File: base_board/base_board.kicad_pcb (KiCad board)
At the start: 6 copper layers, 52 parts, among them J1 Conn_ARM_JTAG_SWD_20, SW1 SW_Push, U1 STM32F446ZEJx, U2 IS42S16400J-xT, U3 BMI270, U4 USB_C_Receptacle_USB2.0, U5 10p, U6 10p, U7 LD3985M33R_SOT23, Y1 Crystal_GND24

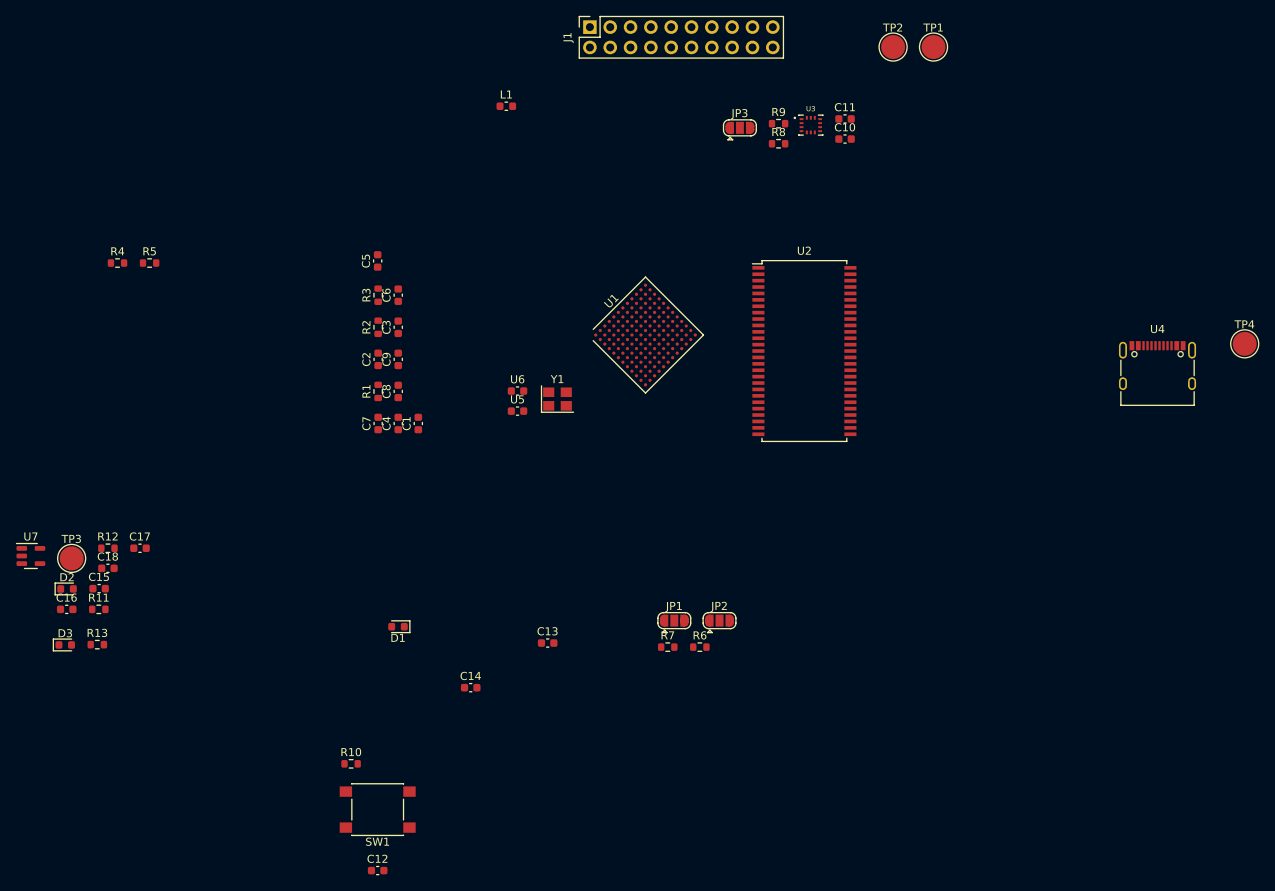
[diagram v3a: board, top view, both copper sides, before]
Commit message: [pcb] draft of components layout
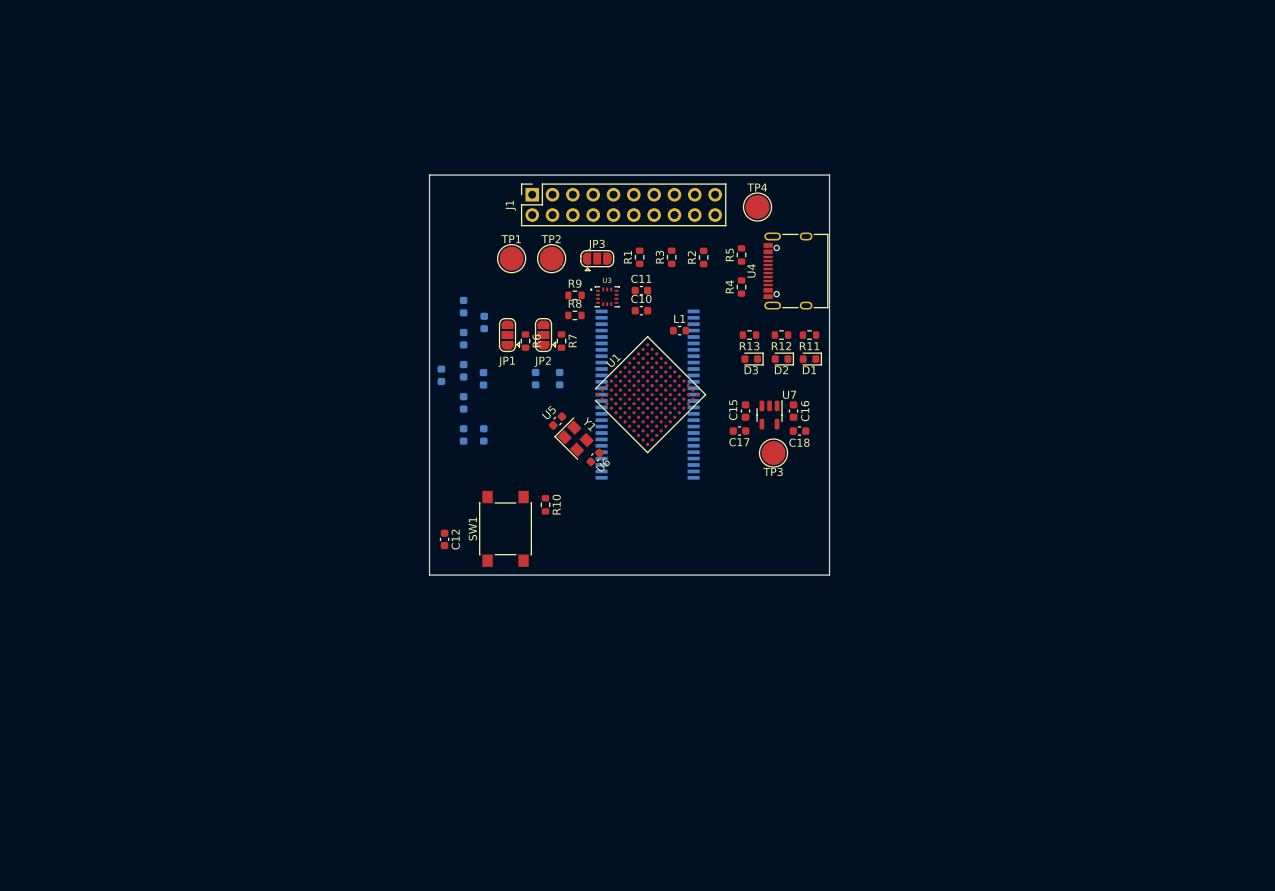
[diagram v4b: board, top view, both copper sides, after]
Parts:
- C1, C13, C14, C2, C3, C4, C5, C6, C7, C8, C9, U2: moved to B.Cu
- moved R11 95.2 mm to (150.5, 88.0), turned to 180 degrees
- moved C16 94.2 mm to (148.5, 97.5), turned to 90 degrees
- moved U7 94.0 mm to (145.5, 98.0), turned to -90 degrees
- moved D2 93.8 mm to (147.0, 91.0), turned to 180 degrees
- moved D3 92.9 mm to (143.2, 91.0), turned to 180 degrees
- moved R13 90.2 mm to (143.0, 88.0), turned to 180 degrees
- moved TP3 88.7 mm to (146.0, 102.8), turned to 180 degrees
- moved R12 88.3 mm to (147.0, 88.0), turned to 180 degrees
- moved C18 88.1 mm to (149.2, 100.0)
- moved C15 83.8 mm to (142.5, 97.5), turned to -90 degrees
- moved R4 78.1 mm to (142.0, 82.0), turned to 90 degrees
- moved C17 76.4 mm to (141.8, 100.0), turned to 180 degrees
- moved R5 74.0 mm to (142.0, 78.0), turned to 90 degrees
- moved TP4 63.3 mm to (144.0, 72.0)
- moved D1 61.4 mm to (150.5, 91.0)
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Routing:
- net /HSE_OUT: track 0.00 -> 0.67 mm
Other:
- board outline added: 50 x 50 mm

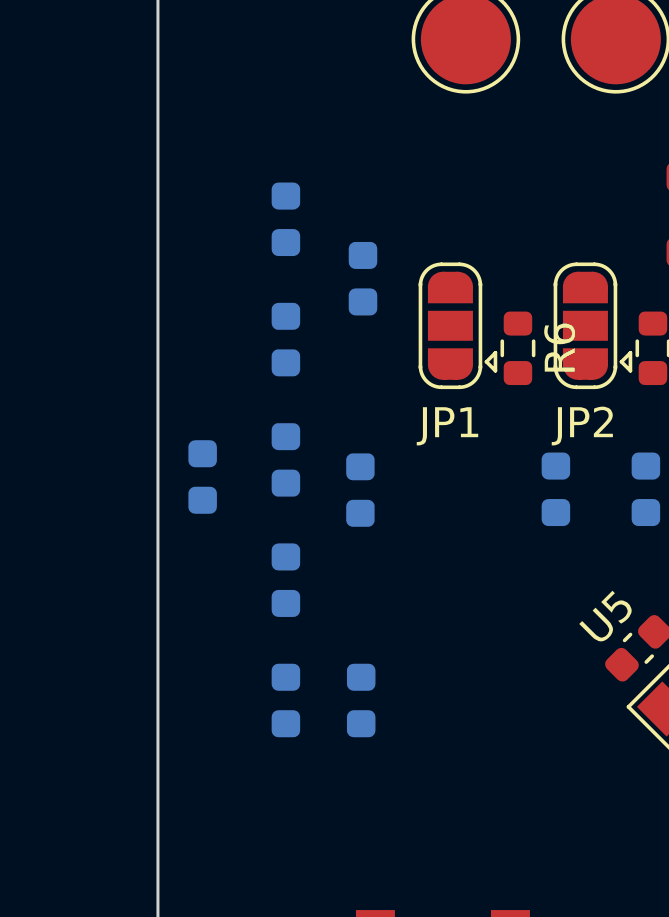
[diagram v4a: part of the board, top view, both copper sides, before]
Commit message: [pcb] changed capacitors layer
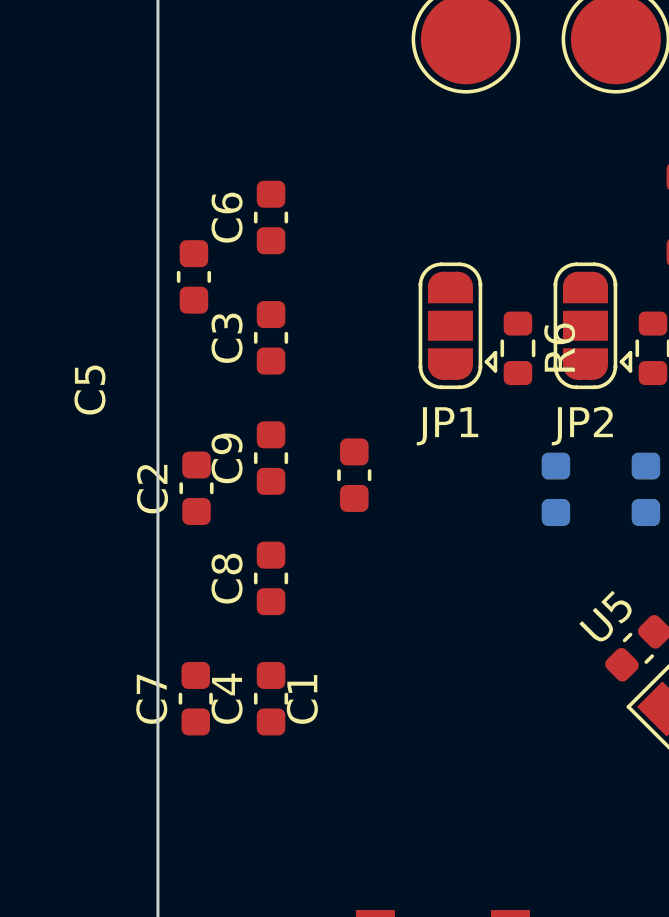
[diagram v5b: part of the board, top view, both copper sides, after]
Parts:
- C1, C2, C3, C4, C5, C6, C7, C8, C9: moved to F.Cu
- moved C5 5.64 mm to (104.2, 86.4)
- moved C7 5.52 mm to (104.3, 100.4)
- moved C2 5.47 mm to (104.3, 93.4)
- moved C1 5.06 mm to (109.5, 93.0)
- moved C6 0.50 mm to (106.8, 84.4)
- moved C8 0.50 mm to (106.8, 96.4)
- moved C9 0.50 mm to (106.8, 92.4)
- moved C3 0.50 mm to (106.8, 88.4)
- moved C4 0.50 mm to (106.8, 100.4)

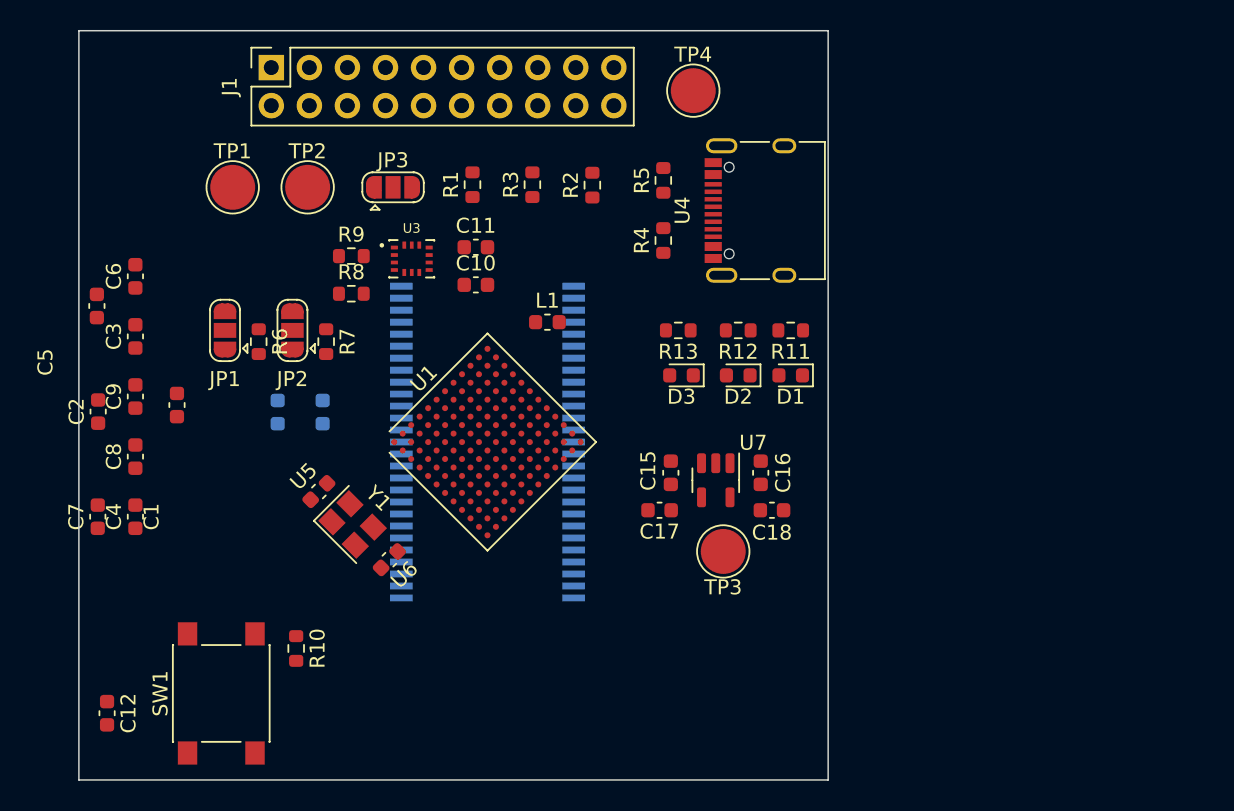
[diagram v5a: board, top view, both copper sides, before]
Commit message: [pcb][schematic] added gpio headers&sockets
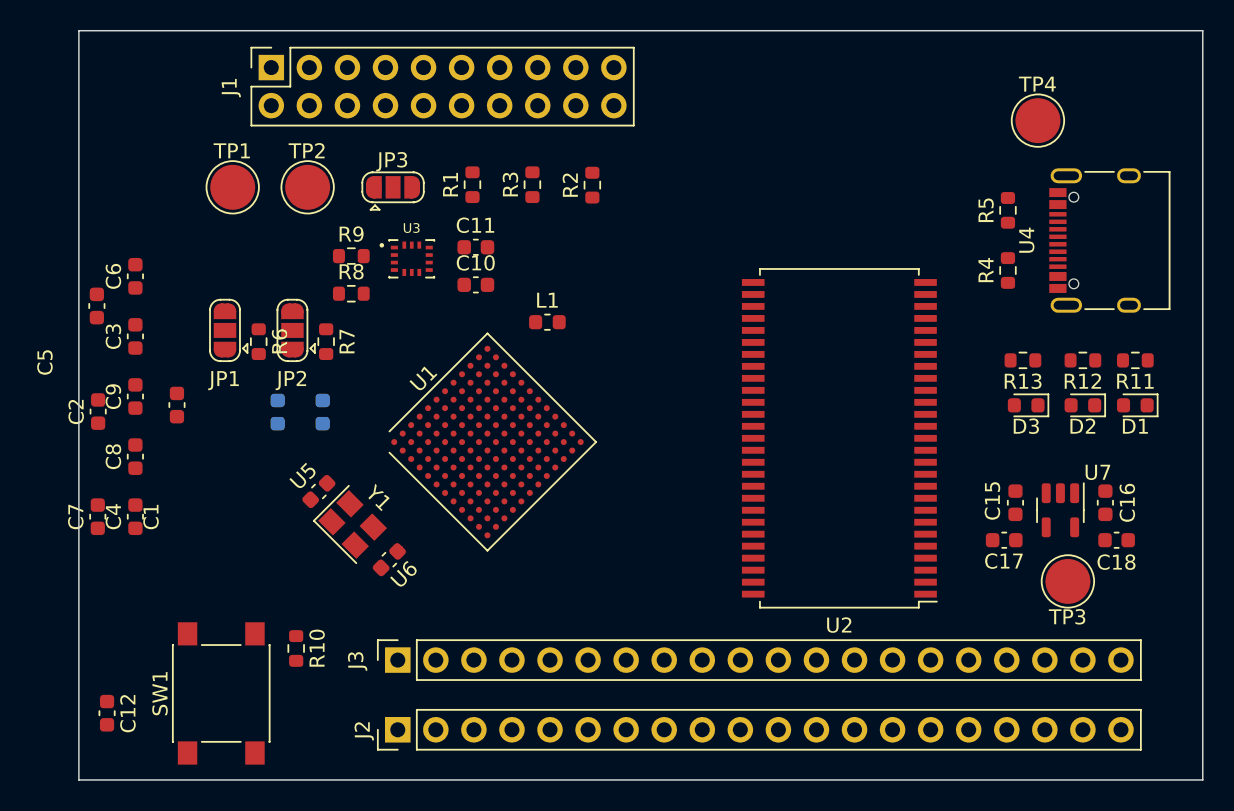
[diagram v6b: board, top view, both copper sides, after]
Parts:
- added J2: Conn_01x20_Pin, Connector_PinHeader_2.54mm:PinHeader_1x20_P2.54mm_Vertical, F.Cu at (124.3, 114.7)
- added J3: Conn_01x20_Socket, Connector_PinSocket_2.54mm:PinSocket_1x20_P2.54mm_Vertical, F.Cu at (124.3, 110.0)
- U2: moved to F.Cu
- moved U2 23.5 mm to (153.8, 95.2), turned to 180 degrees
- moved C15 23.1 mm to (165.5, 99.5)
- moved C16 23.1 mm to (171.5, 99.5)
- moved C17 23.1 mm to (164.8, 102.0)
- moved C18 23.1 mm to (172.2, 102.0)
- moved D1 23.1 mm to (173.5, 93.0)
- moved D2 23.1 mm to (170.0, 93.0)
- moved D3 23.1 mm to (166.2, 93.0)
- moved R11 23.1 mm to (173.5, 90.0)
- moved R12 23.1 mm to (170.0, 90.0)
- moved R13 23.1 mm to (166.0, 90.0)
- moved R4 23.1 mm to (165.0, 84.0)
- moved R5 23.1 mm to (165.0, 80.0)
- moved TP3 23.1 mm to (169.0, 104.8)
- moved TP4 23.1 mm to (167.0, 74.0)
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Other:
- board size 50 x 50 mm -> 75 x 50 mm

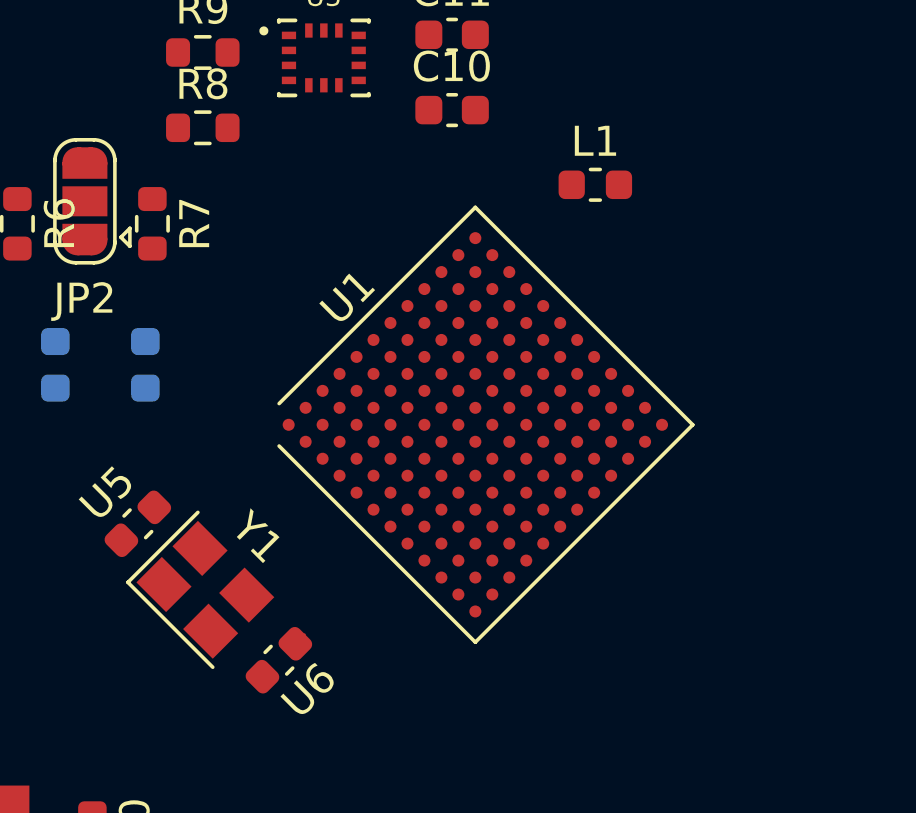
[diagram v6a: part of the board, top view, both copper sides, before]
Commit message: [pcb] added part of bga route
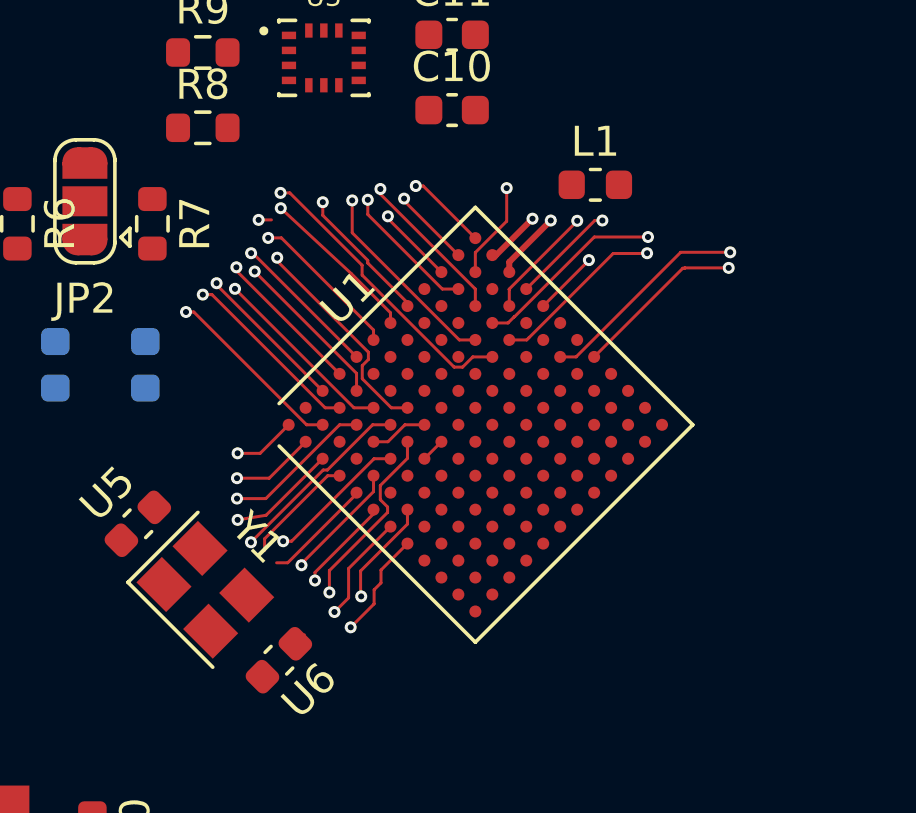
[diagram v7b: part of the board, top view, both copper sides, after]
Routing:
- net /PD2: track 0.00 -> 9.80 mm, vias 0 -> 1
- net /BOOT0: track 0.00 -> 7.29 mm, vias 0 -> 1
- net /FMC_SDCLK: track 0.00 -> 7.11 mm, vias 0 -> 1
- net /PD3: track 0.00 -> 6.66 mm, vias 0 -> 1
- net /FMC_D3: track 0.00 -> 6.40 mm, vias 0 -> 1
- net /FMC_A5: track 0.00 -> 6.30 mm, vias 0 -> 1
- net /FMC_A2: track 0.00 -> 6.27 mm, vias 0 -> 1
- net /FMC_A1: track 0.00 -> 6.26 mm, vias 0 -> 1
- net /PE5: track 0.00 -> 6.12 mm, vias 0 -> 1
- net /PE4: track 0.00 -> 6.11 mm, vias 0 -> 1
- net /FMC_D2: track 0.00 -> 5.79 mm, vias 0 -> 1
- net /FMC_BA1: track 0.00 -> 5.71 mm, vias 0 -> 1
- net /SWO: track 0.00 -> 5.39 mm, vias 0 -> 1
- net /PE6: track 0.00 -> 5.38 mm, vias 0 -> 1
- net /PC12: track 0.00 -> 5.21 mm, vias 0 -> 1
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
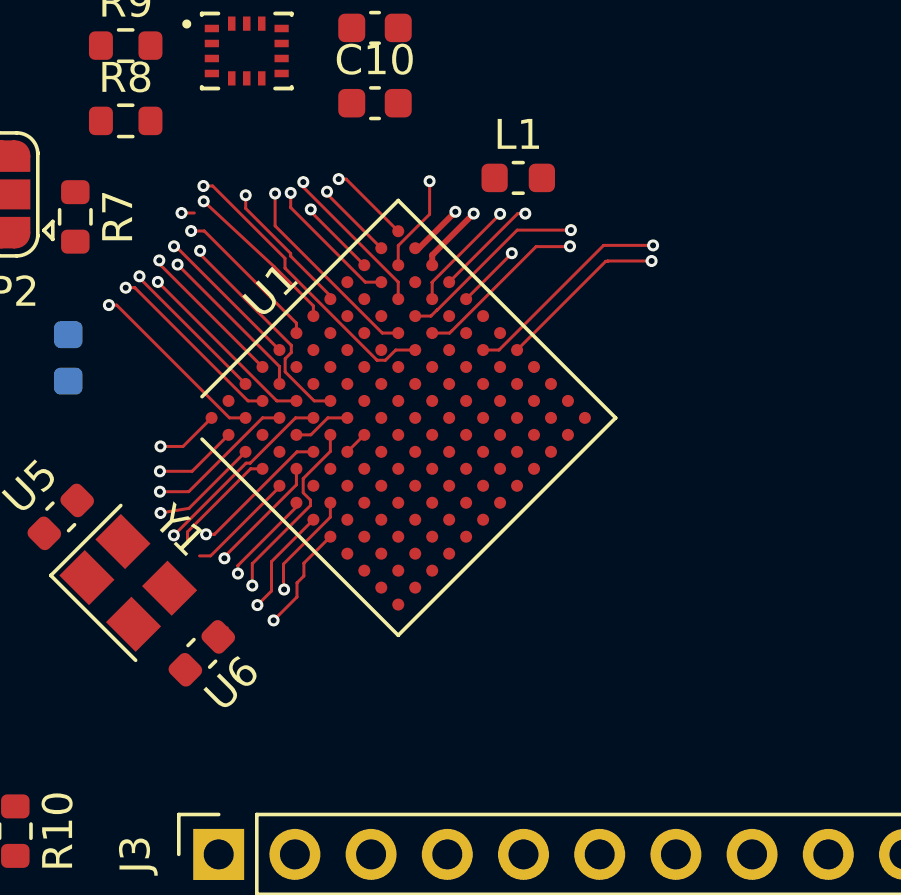
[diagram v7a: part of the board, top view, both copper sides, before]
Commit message: [pcb] added more bga routing
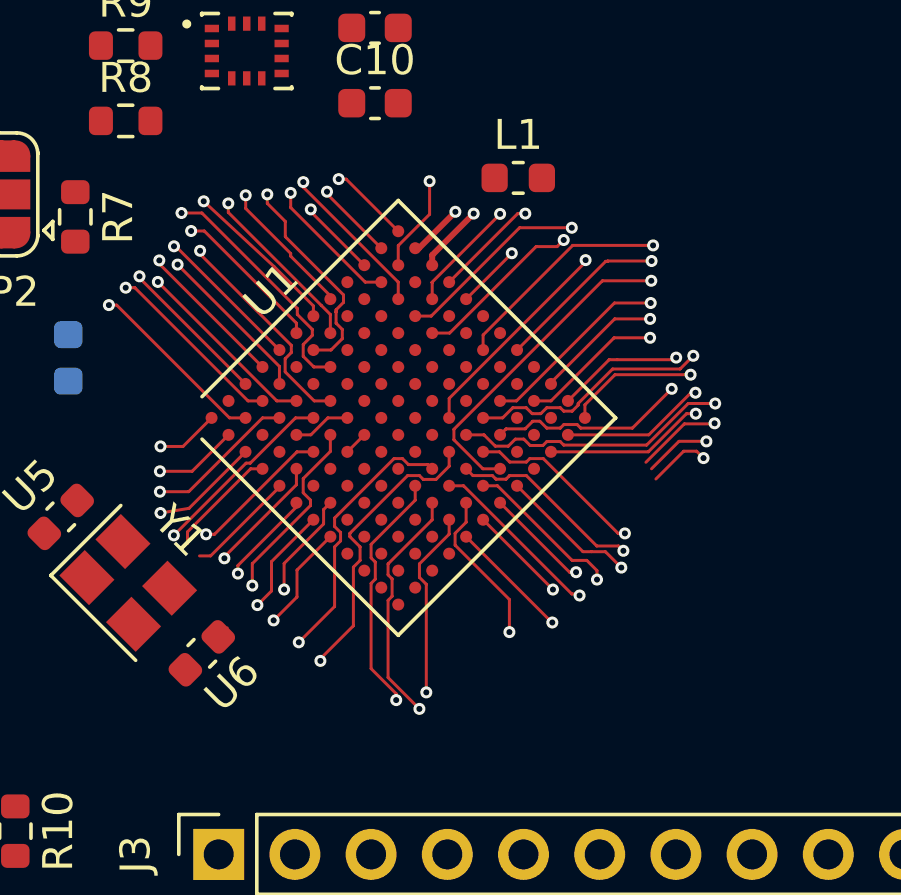
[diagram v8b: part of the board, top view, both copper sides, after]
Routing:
- net /FMC_D11: track 0.00 -> 10.9 mm, vias 0 -> 1
- net /PD2: track 9.80 -> 0.00 mm, vias 1 -> 0
- net /FMC_D7: track 0.00 -> 9.77 mm, vias 0 -> 1
- net /FMC_D9: track 0.00 -> 9.32 mm, vias 0 -> 1
- net /FMC_A11: track 0.00 -> 9.02 mm, vias 0 -> 1
- net /BOOT1: track 0.00 -> 8.22 mm, vias 0 -> 1
- net /FMC_D15: track 0.00 -> 8.16 mm, vias 0 -> 1
- net /FMC_A7: track 0.00 -> 8.03 mm, vias 0 -> 1
- net /FMC_D10: track 0.00 -> 8.01 mm, vias 0 -> 2
- net /FMC_SDNE1: track 0.43 -> 8.16 mm
- net /FMC_SDKE1: track 0.00 -> 7.17 mm, vias 0 -> 1
- net /FMC_D8: track 0.00 -> 7.14 mm, vias 0 -> 1
- net /PD3: track 6.66 -> 0.00 mm, vias 1 -> 0
- net /FMC_D14: track 0.00 -> 6.65 mm, vias 0 -> 1
- net /FMC_D6: track 0.00 -> 6.47 mm, vias 0 -> 1
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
